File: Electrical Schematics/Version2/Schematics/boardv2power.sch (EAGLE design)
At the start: 11 parts, among them U1 LM1085_KTT_3

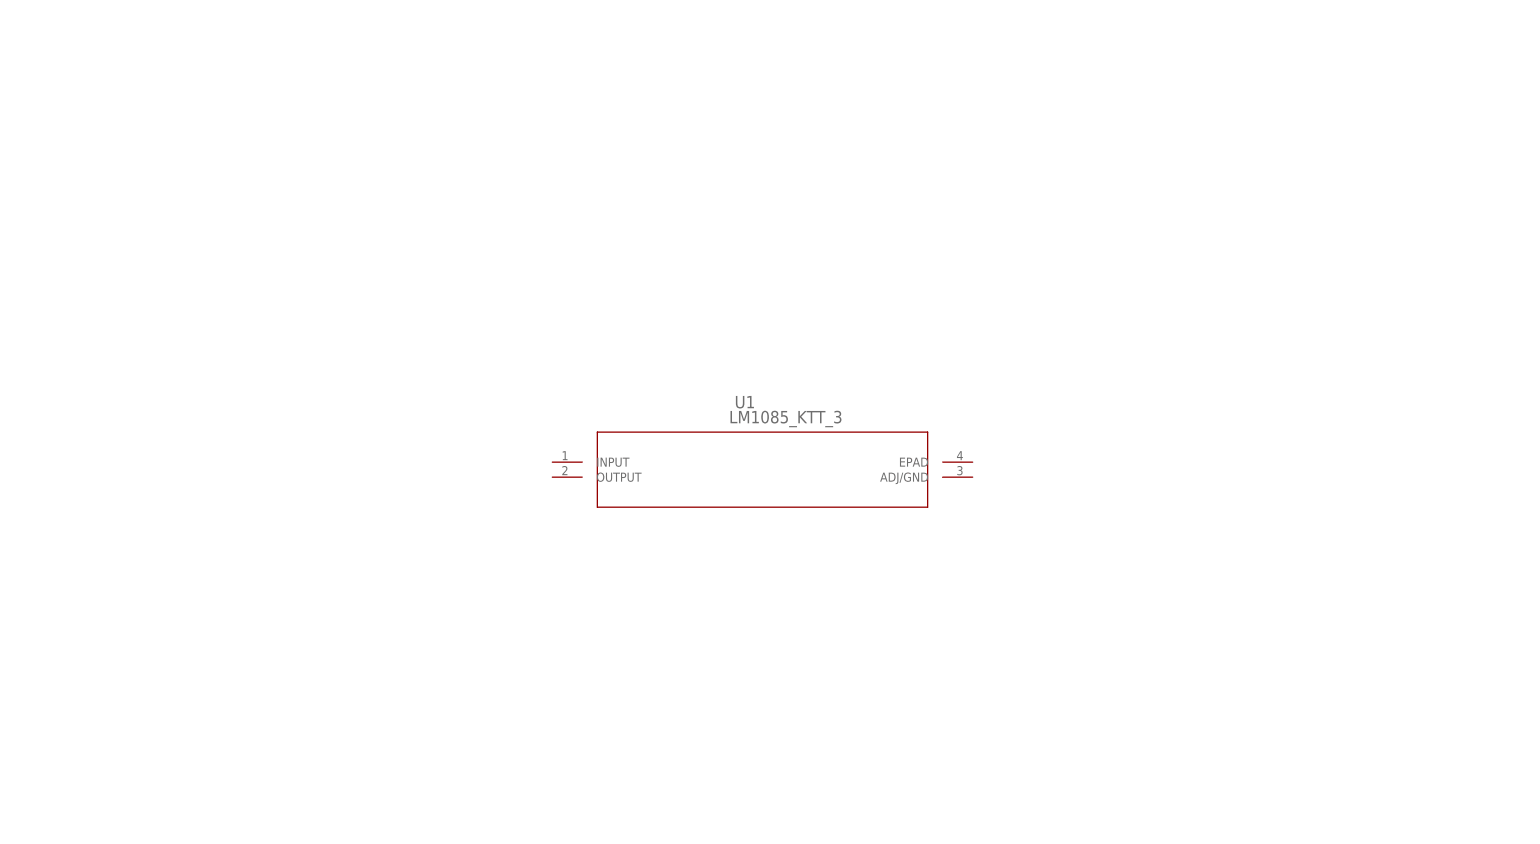
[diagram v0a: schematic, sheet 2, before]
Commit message: power sch update
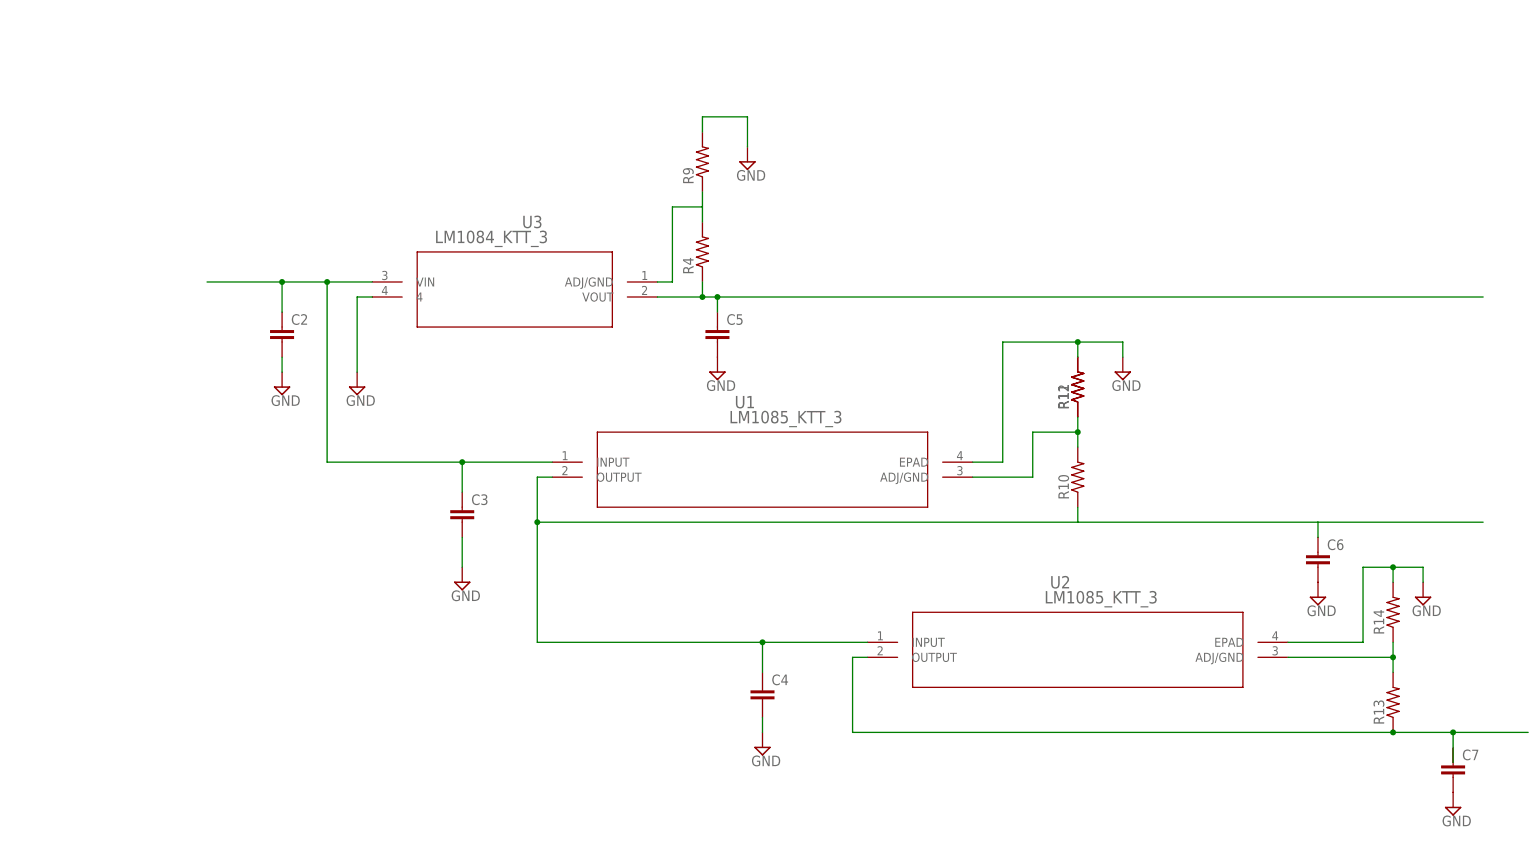
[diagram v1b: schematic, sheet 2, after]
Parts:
- added C2, C3, C4, C5, C6, C7: (no value), eagle-ltspice:CC0603
- added R10, R11, R12, R13, R14, R4, R9: (no value), SparkFun-Passives:RESISTOR0603-RES
- added U2: LM1085_KTT_3, shit:LM1085_KTT_3
- added U3: LM1084_KTT_3, shit:LM1084_KTT_3
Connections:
- new net N$10: C2.1, C3.1, U1.INPUT, U3.VIN
- new net N$11: R4.2, R9.1, U3.ADJ/GND
- new net N$12: C5.1, R4.1, U3.VOUT
- new net N$13: C4.1, C6.1, R10.1, U1.OUTPUT, U2.INPUT
- new net N$14: R13.1, U2.OUTPUT
- new net N$15: R10.2, R12.1, U1.ADJ/GND
- new net N$16: R13.2, R14.1, U2.ADJ/GND
- net GND: now also C2.2, C3.2, C4.2, C5.2, C6.2, C7.2, R12.2, R14.2, R9.2, U1.EPAD, U2.EPAD, U3.4

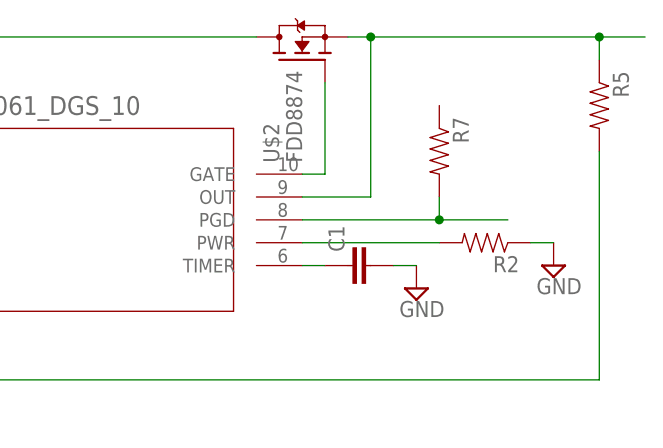
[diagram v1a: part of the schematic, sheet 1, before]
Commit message: Added supervisor part
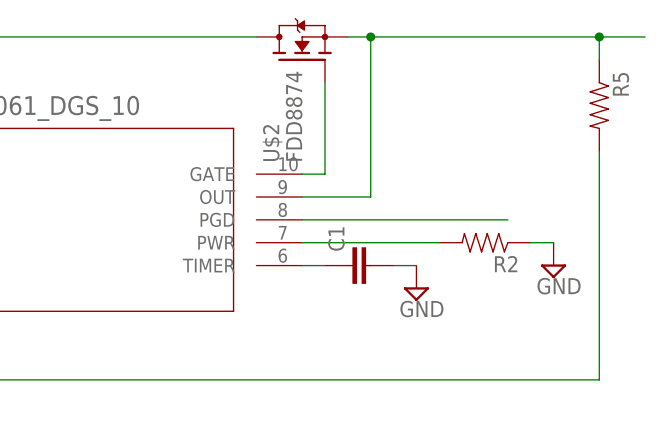
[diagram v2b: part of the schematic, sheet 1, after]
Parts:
- removed R7: (no value), SparkFun-Passives:RESISTOR0603-RES
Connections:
- net N$9: no longer R7.2
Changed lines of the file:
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@@
 <part name="R6" library="SparkFun-Passives" deviceset="RESISTOR" device="0603-RES"/>
 <part name="SUPPLY5" library="supply2" deviceset="GND" device=""/>
-<part name="R7" library="SparkFun-Passives" deviceset="RESISTOR" device="0603-RES"/>
 <part name="U1" library="shit" deviceset="LM1085_KTT_3" device=""/>
 <part name="U2" library="shit" deviceset="LM1085_KTT_3" device=""/>
@@
 <instance part="R6" gate="G$1" x="-22.86" y="17.78" rot="R270"/>
 <instance part="SUPPLY5" gate="GND" x="-22.86" y="7.62"/>
-<instance part="R7" gate="G$1" x="76.2" y="35.56" rot="R270"/>
 </instances>
 <busses>
@@
 <segment>
 <pinref part="U$1" gate="A" pin="PGD"/>
-<wire x1="60.96" y1="27.94" x2="76.2" y2="27.94" width="0.1524" layer="91"/>
-<wire x1="76.2" y1="27.94" x2="83.82" y2="27.94" width="0.1524" layer="91"/>
-<wire x1="76.2" y1="27.94" x2="76.2" y2="30.48" width="0.1524" layer="91"/>
-<pinref part="R7" gate="G$1" pin="2"/>
-<junction x="76.2" y="27.94"/>
+<wire x1="60.96" y1="27.94" x2="83.82" y2="27.94" width="0.1524" layer="91"/>
 </segment>
 </net>

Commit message: Updated Supervisor
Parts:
- added C8: (no value), eagle-ltspice:CC0603
- added R15, R16, R17, R18, R19, R20, R7, R8: (no value), SparkFun-Passives:RESISTOR0603-RES
- added U4: TPS3514_D_14, shit:TPS3514_D_14
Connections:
- new net N$17: R7.2, R8.2, U4.PGI
- new net N$18: R8.1
- new net N$19: C8.2, R18.2, U4.VS12
- new net N$20: R15.2, U4.RI
- new net N$21: R16.1, R18.1
- new net N$22: R17.2, U4.*FPO
- new net N$24: R17.1, U4.VDD
- new net N$25: U4.*PSON
- new net N$26: R19.1, R20.2
- new net N$27: C8.1, R16.2, U4.IS12
- new net N$28: R20.1, U4.IS5
- new net N$29: R19.2, U4.VS5
- net GND: now also R15.1, R7.1, U4.GND
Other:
- note added: "12V"
- note added: "5V"
- note added: "5V VSB"
- note added: "PG"

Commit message: updated power ethernet and tempatature
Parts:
- added C10, C9: (no value), eagle-ltspice:CC0603
- added R21, R22, R23, R24, R25, R26, R27, R28, R29, R30, RS1, RS2: (no value), SparkFun-Passives:RESISTOR0603-RES
- added U$3, U$5: LM25061_DGS_10, shit:LM25061_DGS_10
- added U$4, U$6: FDD8874, transistor-fet:FDD8874
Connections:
- new net N$30: C9.1, U$3.TIMER
- new net N$31: R22.2, U$3.PWR
- new net N$32: R21.2, R23.2, U$3.UVLO/EN
- new net N$33: RS1.1, U$3.SENSE, U$4.D
- new net N$34: R21.1, RS1.2, U$3.VIN
- new net N$35: U$3.GATE, U$4.G
- new net N$36: R24.2, R25.1, U$3.FB
- new net N$37: R24.1, U$3.OUT, U$4.S
- new net N$38: U$3.PGD
- new net N$39: C10.1, U$5.TIMER
- new net N$40: R27.2, U$5.PWR
- new net N$41: R26.2, R28.2, U$5.UVLO/EN
- new net N$42: RS2.1, U$5.SENSE, U$6.D
- new net N$43: R26.1, RS2.2, U$5.VIN
- new net N$44: U$5.GATE, U$6.G
- new net N$45: R29.2, R30.1, U$5.FB
- new net N$46: R29.1, U$5.OUT, U$6.S
- new net N$47: U$5.PGD
- net GND: now also C10.2, C9.2, R22.1, R23.1, R25.2, R27.1, R28.1, R30.2, U$3.GND, U$5.GND

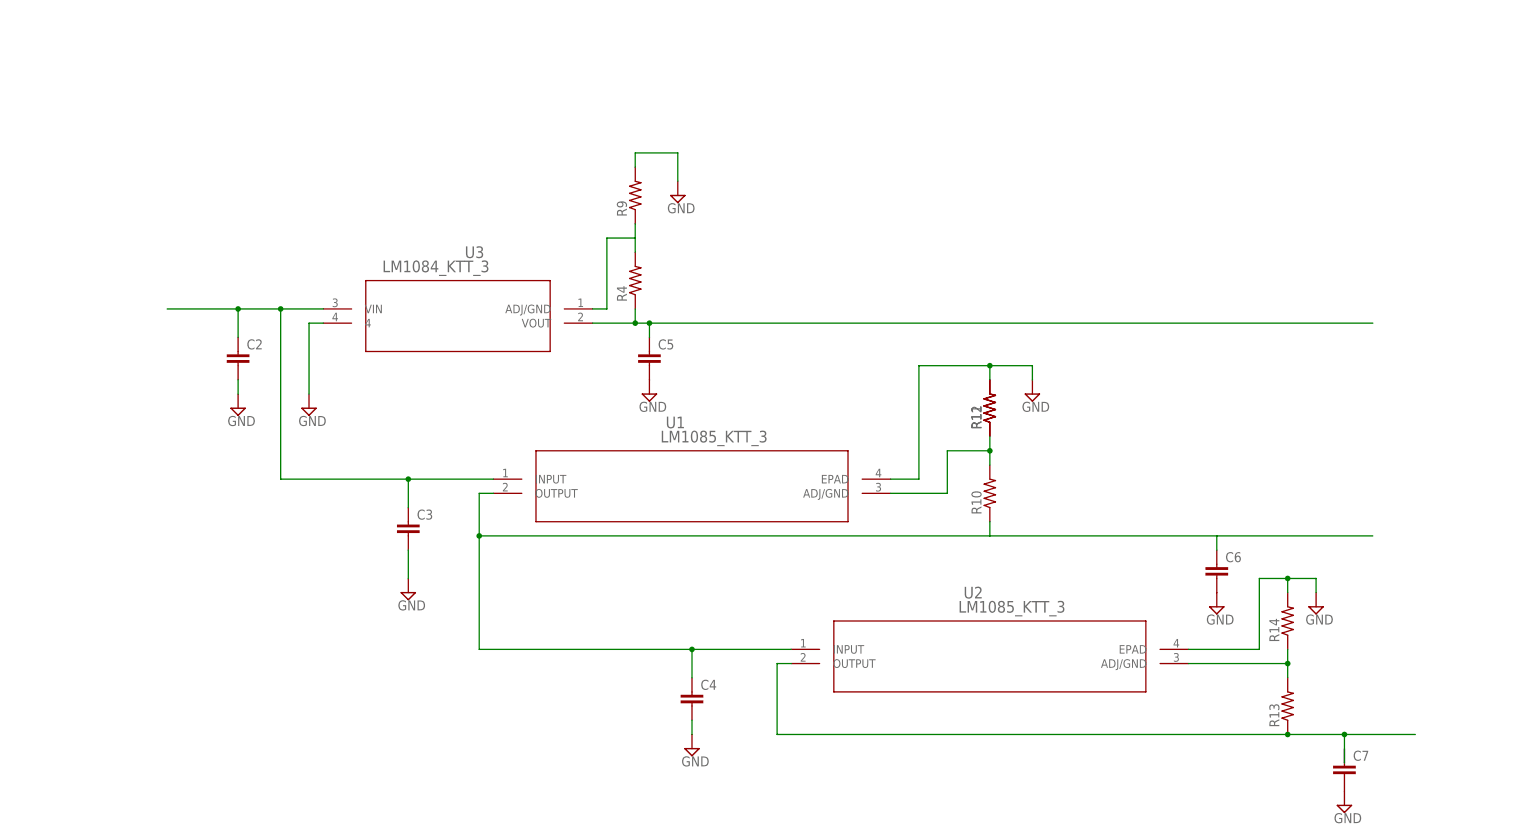
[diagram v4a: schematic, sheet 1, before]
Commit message: updated the schematics for the ridgley
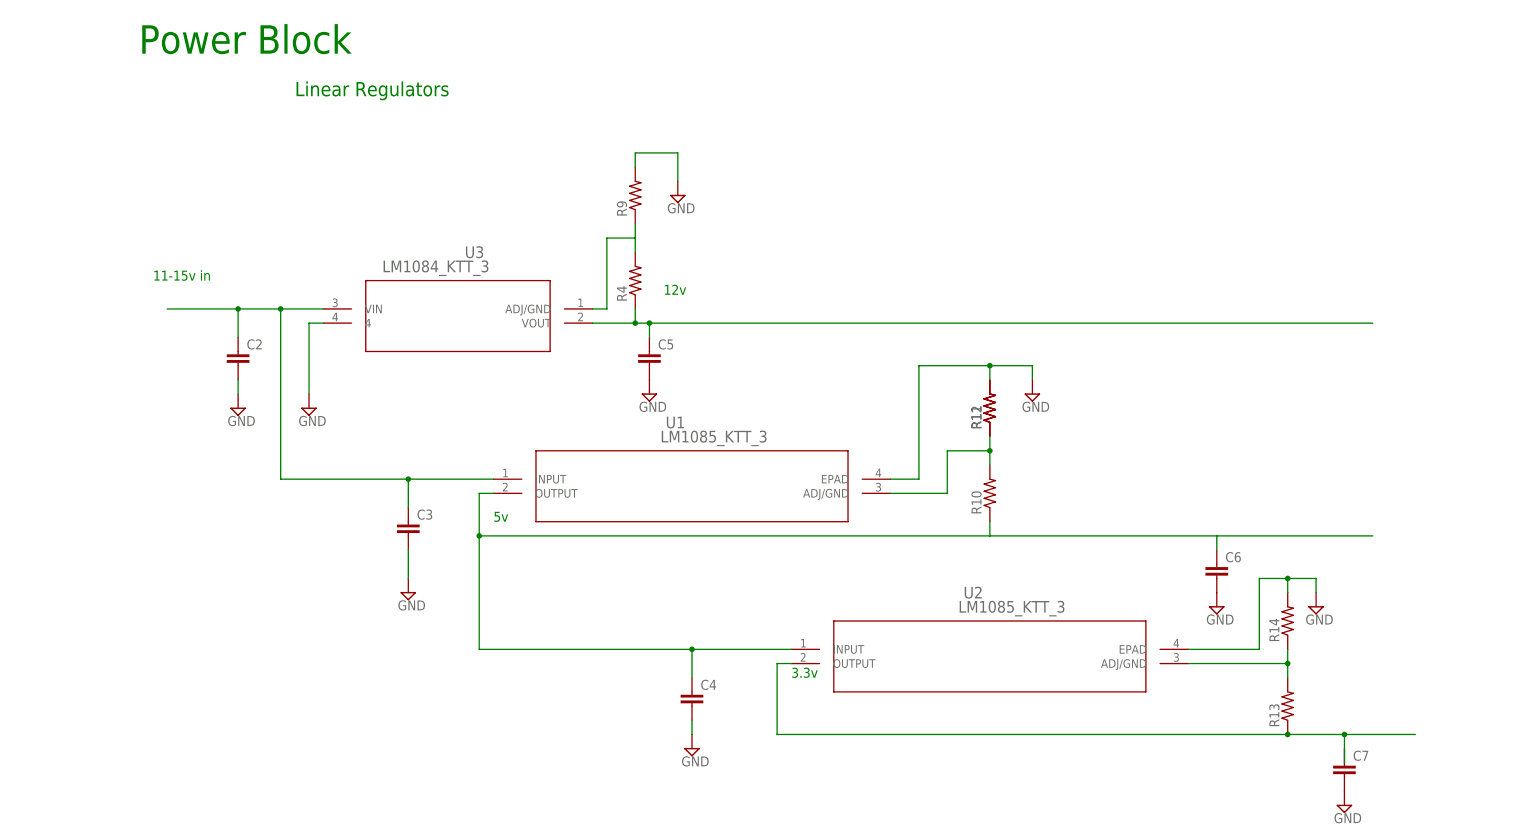
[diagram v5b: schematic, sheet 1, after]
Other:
- note added: "11-15v in"
- note added: "12v"
- note added: "3.3v"
- note added: "3.3v 5v 12v power supervisor Watches all the lines voltages and current draw"
- note added: "5v"
- note added: "Linear Regulators"
- note added: "Power Block"
- note added: "Protection circuit for the Battery Monitoring Circuit"
- note added: "Protection circuit for the FPGA"
- note added: "Protection circuit for the mcu"
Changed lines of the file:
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@@
 <part name="R30" library="SparkFun-Passives" deviceset="RESISTOR" device="0603-RES"/>
 <part name="SUPPLY26" library="supply2" deviceset="GND" device=""/>
+<part name="FRAME1" library="frames" deviceset="DOCFIELD" device=""/>
+<part name="FRAME2" library="frames" deviceset="DOCFIELD" device=""/>
+<part name="FRAME3" library="frames" deviceset="DOCFIELD" device=""/>
+<part name="FRAME4" library="frames" deviceset="DOCFIELD" device=""/>
+<part name="FRAME5" library="frames" deviceset="DOCFIELD" device=""/>
 </parts>
 <sheets>
@@
 <description>Regulators</description>
 <plain>
+<text x="-20.32" y="91.44" size="1.778" layer="91">11-15v in</text>
+<text x="71.12" y="88.9" size="1.778" layer="91">12v</text>
+<text x="40.64" y="48.26" size="1.778" layer="91">5v</text>
+<text x="93.98" y="20.32" size="1.778" layer="91">3.3v</text>
+<frame x1="-30.48" y1="-50.8" x2="325.12" y2="147.32" columns="8" rows="5" layer="91"/>
+<text x="5.08" y="124.46" size="2.54" layer="91">Linear Regulators</text>
+<text x="-22.86" y="132.08" size="5.08" layer="91">Power Block</text>
 </plain>
 <instances>
@@
 <instance part="C7" gate="G$1" x="193.04" y="5.08"/>
 <instance part="SUPPLY15" gate="GND" x="193.04" y="-2.54"/>
+<instance part="FRAME1" gate="G$1" x="218.44" y="-45.72"/>
 </instances>
 <busses>
@@
 <text x="-43.18" y="71.12" size="1.778" layer="91">5V VSB</text>
 <text x="-38.1" y="81.28" size="1.778" layer="91">5V</text>
+<frame x1="-63.5" y1="-27.94" x2="218.44" y2="137.16" columns="8" rows="5" layer="91"/>
+<text x="-50.8" y="124.46" size="5.08" layer="91">Power Block</text>
+<text x="-50.8" y="119.38" size="2.54" layer="91">3.3v 5v 12v power supervisor Watches all the lines voltages and current draw</text>
 </plain>
 <instances>
@@
 <instance part="R19" gate="G$1" x="124.46" y="81.28"/>
 <instance part="R20" gate="G$1" x="104.14" y="40.64"/>
+<instance part="FRAME2" gate="G$1" x="111.76" y="-22.86"/>
 </instances>
 <busses>
@@
 <description>Power Monitoring Circuit MCU</description>
 <plain>
+<frame x1="-63.5" y1="-48.26" x2="132.08" y2="71.12" columns="8" rows="5" layer="91"/>
+<text x="-55.88" y="58.42" size="5.08" layer="91">Power Block</text>
+<text x="-55.88" y="53.34" size="1.778" layer="91">Protection circuit for the mcu</text>
 </plain>
 <instances>
@@
 <instance part="R6" gate="G$1" x="-22.86" y="17.78" rot="R270"/>
 <instance part="SUPPLY5" gate="GND" x="-22.86" y="7.62"/>
+<instance part="FRAME3" gate="G$1" x="25.4" y="-43.18"/>
 </instances>
 <busses>
@@
 <description>Power monitoring  BM</description>
 <plain>
+<frame x1="-27.94" y1="-7.62" x2="167.64" y2="111.76" columns="8" rows="5" layer="91"/>
+<text x="-20.32" y="99.06" size="5.08" layer="91">Power Block</text>
+<text x="-20.32" y="91.44" size="1.778" layer="91">Protection circuit for the FPGA</text>
 </plain>
 <instances>
@@
 <instance part="R25" gate="G$1" x="2.54" y="50.8" rot="R270"/>
 <instance part="SUPPLY21" gate="GND" x="2.54" y="40.64"/>
+<instance part="FRAME4" gate="G$1" x="60.96" y="-2.54"/>
 </instances>
 <busses>
@@
 <description>power monitoring FPGA</description>
 <plain>
+<frame x1="-22.86" y1="-2.54" x2="172.72" y2="116.84" columns="8" rows="5" layer="91"/>
+<text x="-15.24" y="104.14" size="5.08" layer="91">Power Block</text>
+<text x="-15.24" y="96.52" size="1.778" layer="91">Protection circuit for the Battery Monitoring Circuit</text>
 </plain>
 <instances>
@@
 <instance part="R30" gate="G$1" x="5.08" y="50.8" rot="R270"/>
 <instance part="SUPPLY26" gate="GND" x="5.08" y="40.64"/>
+<instance part="FRAME5" gate="G$1" x="66.04" y="2.54"/>
 </instances>
 <busses>

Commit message: updated power circuit
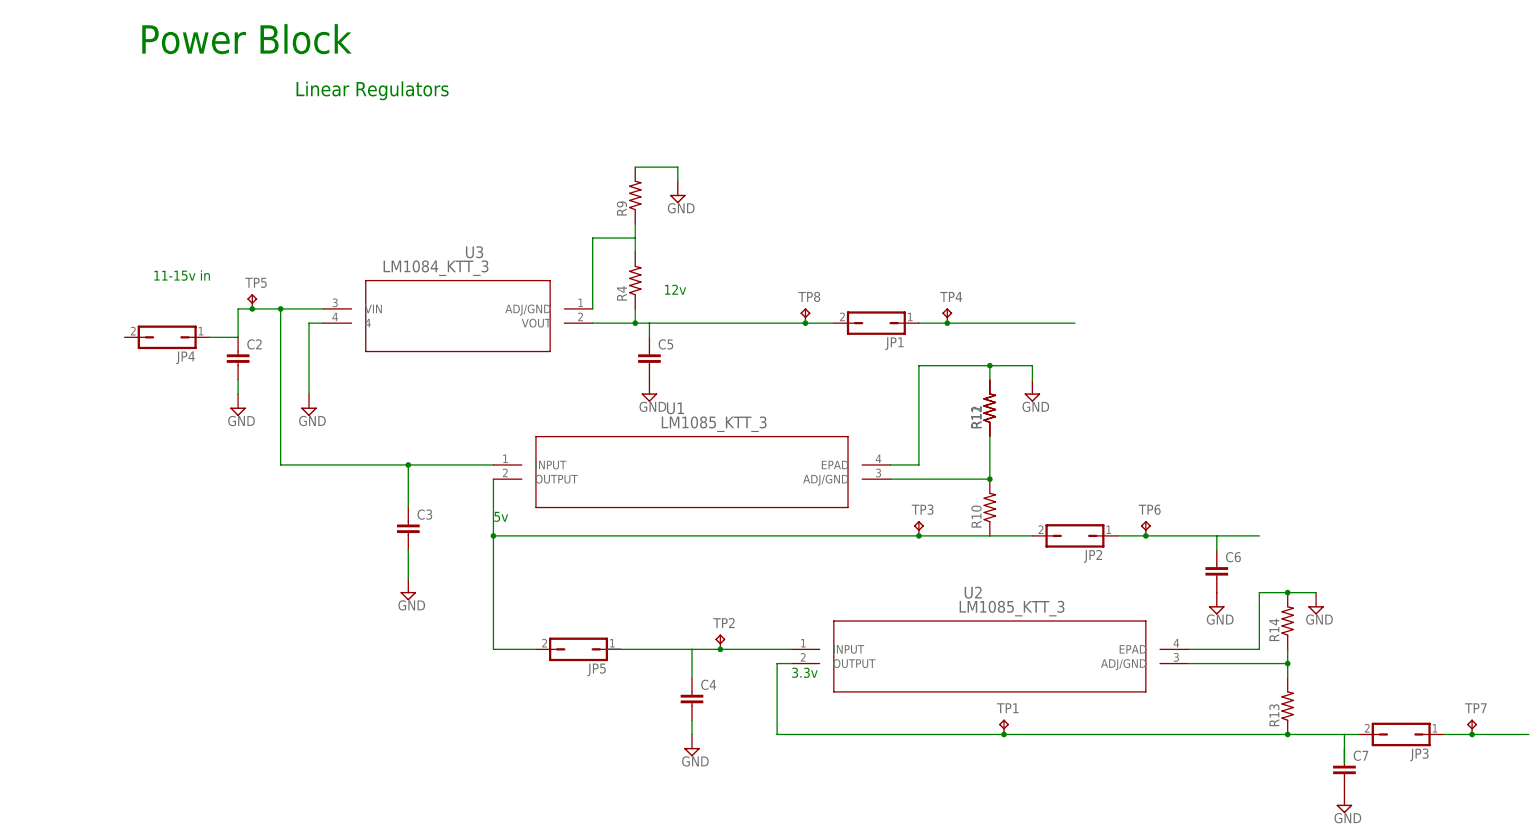
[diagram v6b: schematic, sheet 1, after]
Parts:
- added JP1, JP2, JP3, JP4, JP5: (no value), jumper:JP1Q
- added TP1, TP2, TP3, TP4, TP5, TP6, TP7, TP8: TPB1,27, testpad:TPB1,27
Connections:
- new net N$49: JP1.1, TP4.TP
- new net N$50: C6.1, JP2.1, TP6.TP
- new net N$51: JP3.1, TP7.TP
- new net N$52: C4.1, TP2.TP, U2.INPUT
- net N$10: now also JP4.1, TP5.TP
- net N$12: now also JP1.2, TP8.TP
- net N$13: now also JP2.2, JP5.2, TP3.TP; no longer C4.1, C6.1, U2.INPUT
- net N$14: now also JP3.2, TP1.TP
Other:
- moved on the sheet: R10, U1
